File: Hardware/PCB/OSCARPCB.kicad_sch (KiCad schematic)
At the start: 9 parts, among them J2 Stepper Motor OUT, J3 DC Motors OUT, J4 Servo OUT, J5 Power Input, J6 PINHD_1x2_Female, U1 L293D, U2 ESP32-DevKitC

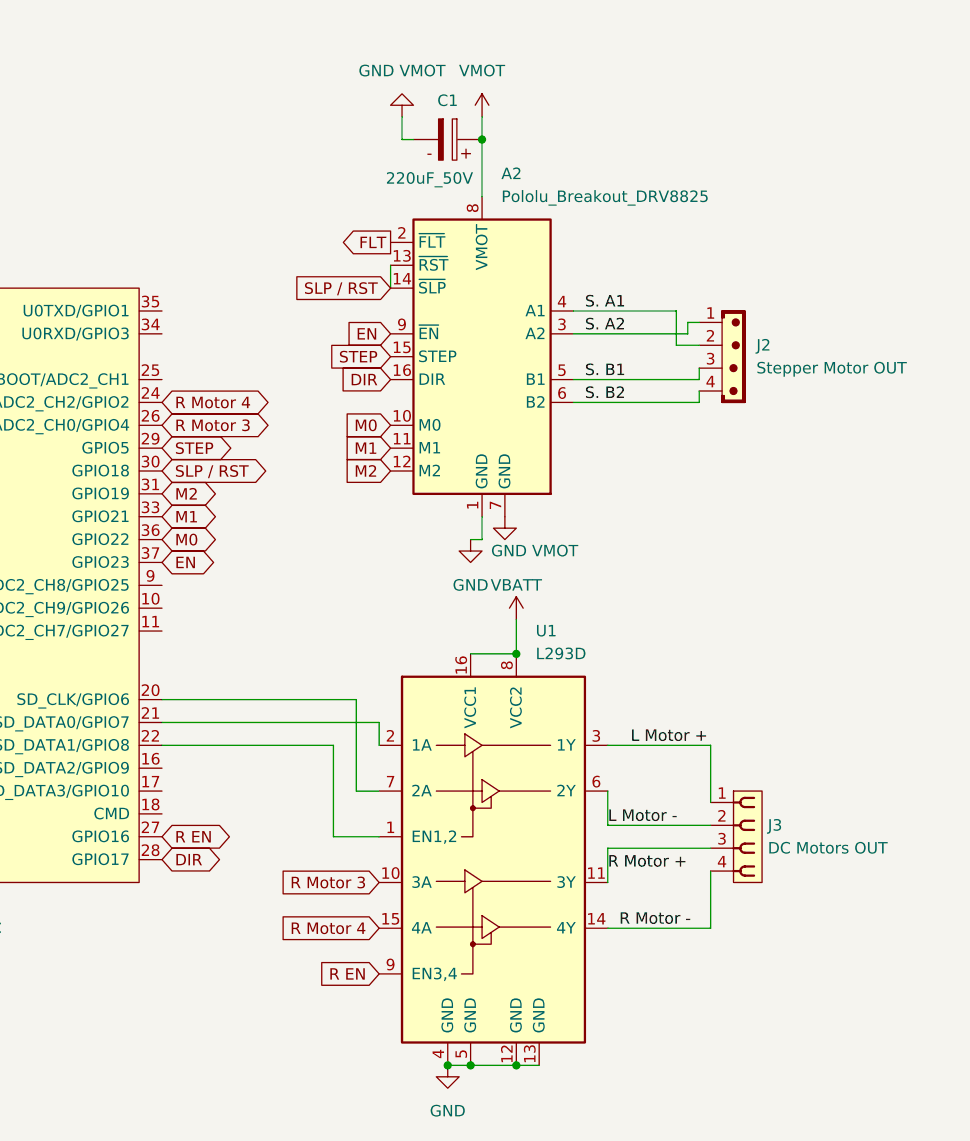
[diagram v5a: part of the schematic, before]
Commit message: Updated PCB becasue Im using external components
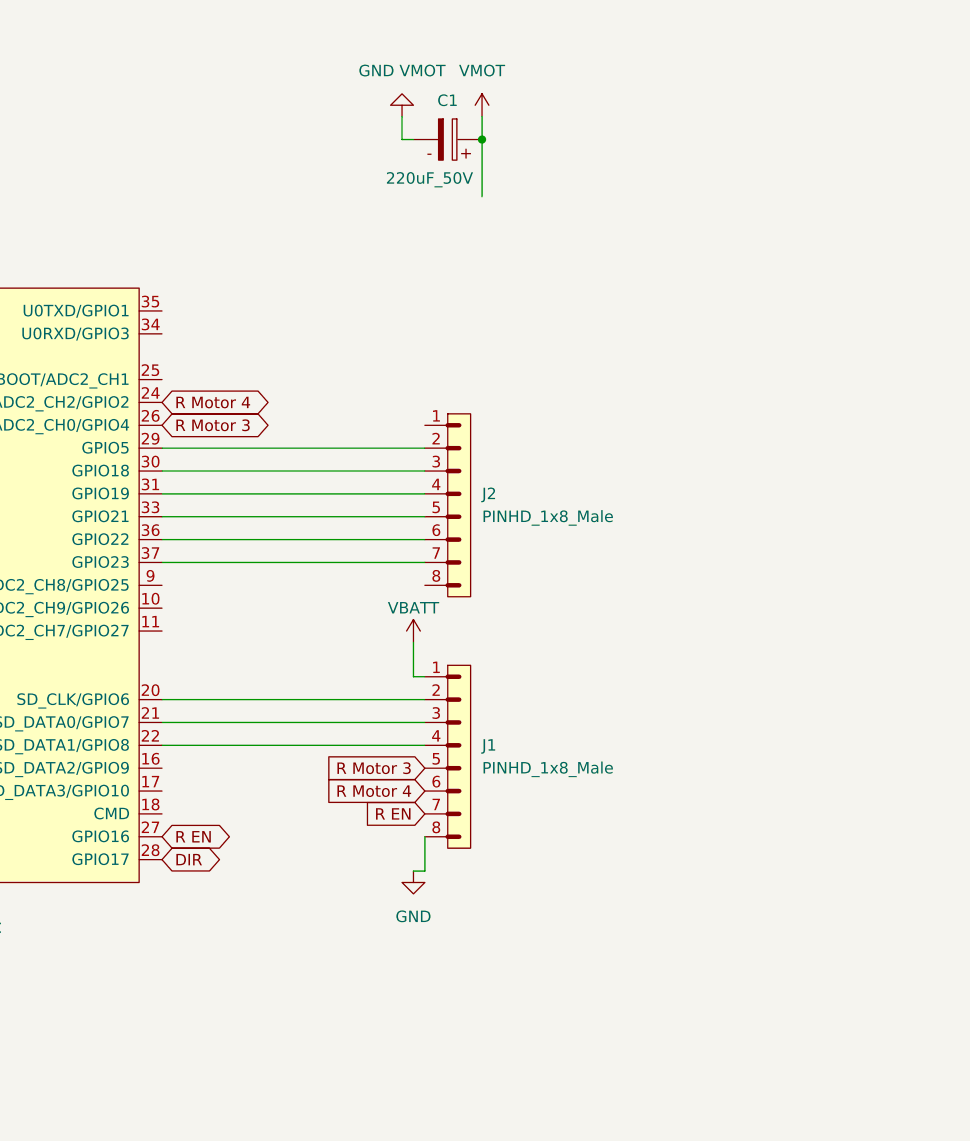
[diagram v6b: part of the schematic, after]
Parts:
- removed A2: Pololu_Breakout_DRV8825, Module:Pololu_Breakout-16_15.2x20.3mm, symbol Driver_Motor:Pololu_Breakout_DRV8825
- removed J2: Stepper Motor OUT, Connector_JST:JST_EH_B4B-EH-A_1x04_P2.50mm_Vertical, symbol PCM_SL_Connectors:JST_04
- removed J3: DC Motors OUT, Connector_PinSocket_2.54mm:PinSocket_1x04_P2.54mm_Vertical, symbol PCM_SL_Pin_Headers:PINHD_1x4_Female
- removed U1: L293D, Package_DIP:DIP-16_W7.62mm, symbol Driver_Motor:L293D
- added J1, J2: PINHD_1x8_Male, Connector_PinHeader_2.54mm:PinHeader_1x08_P2.54mm_Vertical, symbol PCM_SL_Pin_Headers:PINHD_1x8_Male
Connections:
- net GND: now also J1.8
- net R EN: now also J1.7
- net R Motor 3: now also J1.5
- net R Motor 4: now also J1.6
- net VBATT: now also J1.1
- net at U2.20 (SD_CLK/GPIO6): now also J1.2
- net at U2.21 (SD_DATA0/GPIO7): now also J1.3
- net at U2.22 (SD_DATA1/GPIO8): now also J1.4
- net EN: no longer names the net of U2.37 (GPIO23)
- net EN: now also J2.7
- net M0: no longer names the net of U2.36 (GPIO22)
- net M0: now also J2.6
- net M1: no longer names the net of U2.33 (GPIO21)
- net M1: now also J2.5
- net M2: no longer names the net of U2.31 (GPIO19)
- net M2: now also J2.4
- net SLP / RST: no longer names the net of U2.30 (GPIO18)
- net SLP / RST: now also J2.3
- net STEP: no longer names the net of U2.29 (GPIO5)
- net STEP: now also J2.2

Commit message: PCB Done?
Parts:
- removed C1: 220uF_50V, Capacitor_THT:CP_Radial_D10.0mm_P5.00mm, symbol PCM_SL_Capacitors:220uF_50V
- J1, J2: footprint Connector_PinHeader_2.54mm:PinHeader_1x08_P2.54mm_Vertical -> Connector_PinHeader_2.54mm:PinHeader_1x06_P2.54mm_Vertical; symbol PCM_SL_Pin_Headers:PINHD_1x8_Male -> PCM_SL_Pin_Headers:PINHD_1x6_Male
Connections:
- net GND: no longer J1.8
- net R EN: now also J1.6, U2.10 (DAC_2/ADC2_CH9/GPIO26); no longer J1.7, U2.27 (GPIO16)
- net R Motor 3: now also J1.4, U2.8 (32K_XN/GPIO33/ADC1_CH5); no longer J1.5, U2.26 (ADC2_CH0/GPIO4)
- net R Motor 4: now also J1.5, U2.9 (DAC_1/ADC2_CH8/GPIO25); no longer J1.6, U2.24 (ADC2_CH2/GPIO2)
- net VBATT: no longer J1.1
- net at J2.1: now also U2.29 (GPIO5)
- net at J2.2: now also U2.30 (GPIO18); no longer U2.29 (GPIO5)
- net at J2.3: now also U2.31 (GPIO19); no longer U2.30 (GPIO18)
- net at J2.4: now also U2.33 (GPIO21); no longer U2.31 (GPIO19)
- net at J2.5: now also U2.36 (GPIO22); no longer U2.33 (GPIO21)
- net at J2.6: now also U2.37 (GPIO23); no longer U2.36 (GPIO22)
- net at U2.20 (SD_CLK/GPIO6): no longer J1.2
- net at U2.21 (SD_DATA0/GPIO7): no longer J1.3
- net at U2.22 (SD_DATA1/GPIO8): no longer J1.4
- net L Motor EN: now reaches U2.5 (VDET_1/GPIO34/ADC1_CH6)
- net L Motor EN: now also J1.1
- net L Motor 1: now reaches U2.6 (VDET_2/GPIO35/ADC1_CH7)
- net L Motor 1: now also J1.2
- net L Motor 2: now reaches U2.7 (32K_XP/GPIO32/ADC1_CH4)
- net L Motor 2: now also J1.3
- net DIR: no longer names the net of U2.28 (GPIO17)
